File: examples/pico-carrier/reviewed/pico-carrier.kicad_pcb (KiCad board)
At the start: 2 copper layers, 88 x 62 mm, 9 parts, among them J1 5V IN, J3 GP0-GP15, J4 GP16-GP28, PWR, U1 Pico

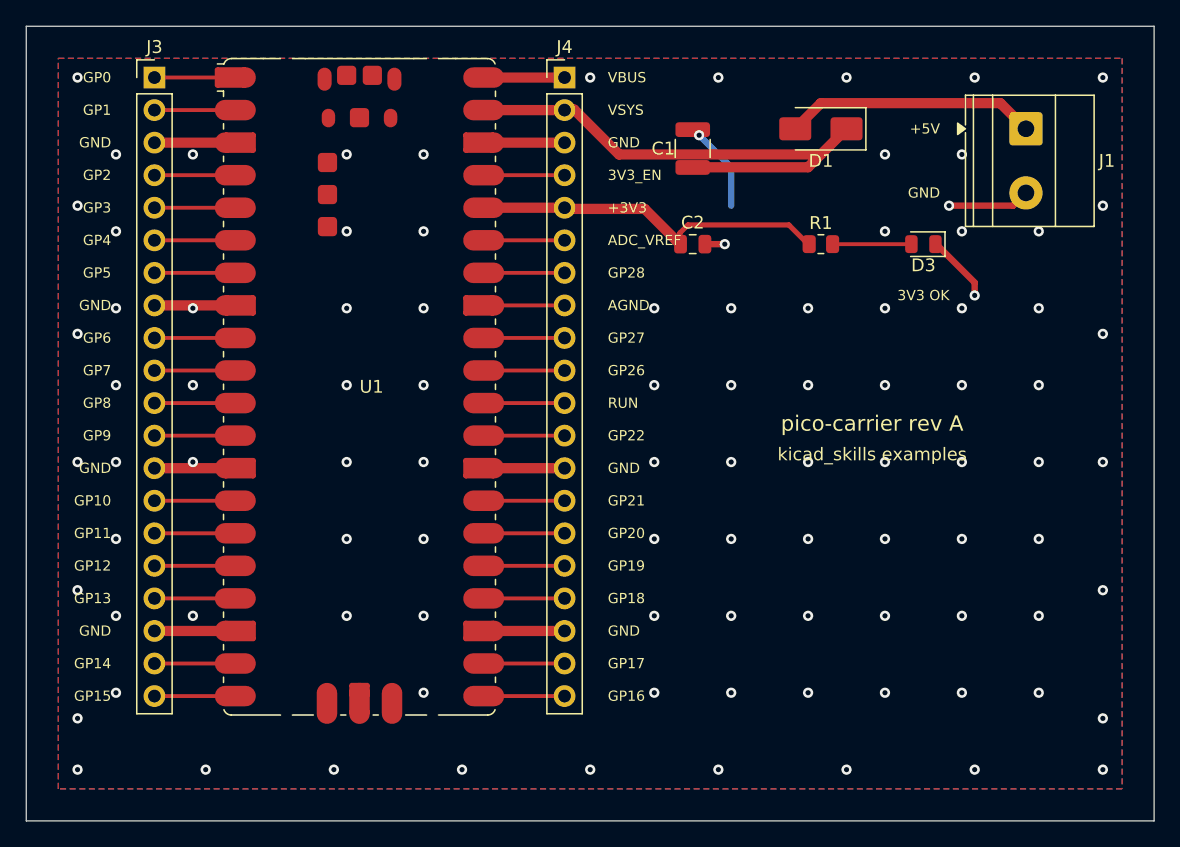
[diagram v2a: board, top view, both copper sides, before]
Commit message: Learn the drawing from the boards people drew
The brief for this round: relying on the autorouter and the numbers alone is
not enough - organise what pictorial correctness looks like from ordinary
circuits and open designs, and improve the drawing itself. So it starts in
KiCad's own demo corpus, measured and looked at, and ends with the habits
pushed into the generator.

tools/board_signature.py (new) reduces "looks autorouted" to five numbers.
Hand-routed two-layer boards cluster tightly: 10-47% of copper on the second
face, median segments 1.8-3.5 mm, 9-25 corners per decimetre, 91-98% of them
45s, 0.3-16 vias per decimetre. Rendering interf_u beside our boards says the
same thing in one glance: a layer has a direction, a bus travels as a bundle,
a person covers an offset with the long straight and one diagonal.

Three habits, now in the generator:

* Router.route(follow=...): cells beside a sibling net's path are discounted,
  so a bus (nets sharing a name prefix - I2S_*, SPI_*) travels as parallel
  lanes in one corridor. The discount is a fraction of a step, so it never
  buys a detour.
* _doglegged: every wiggly stretch is redrawn as the human stroke - the
  straight along the dominant direction plus one 45 - when the dogleg is
  clear, recursing into halves where a crossing blocks the whole. The op-amp
  board's median segment rose from 0.75 mm and its corner rate fell from
  38/dm; the FPGA board landed at 1.54 mm and 17.8/dm, inside the human band.
* Purposeful stitching: the 6 mm via carpet is gone. A ring at the rim, vias
  beside every back-layer crossing (where the plane is actually cut), and a
  coarse 12 mm mesh so no pour orphans. Vias/dm: buck 41 -> 18, carrier
  28 -> 13, all five inside the corpus band, pour_fragmented still silent.

Three failures the round produced and what they taught:

* pinned(): reshaping may not move copper off any point inside an own-net
  pad - the centre alone was not enough, a routed run touches off-centre and
  the ove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
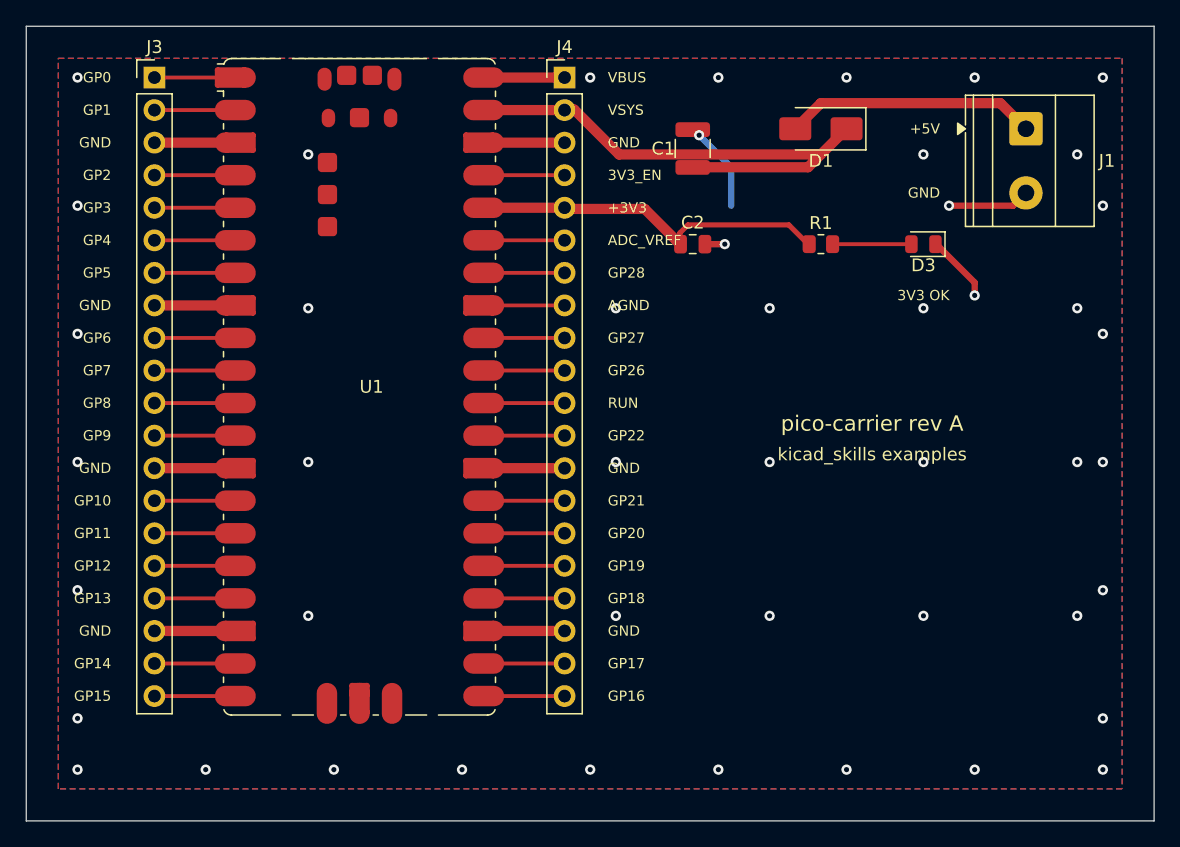
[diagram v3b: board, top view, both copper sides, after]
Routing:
- net GND: vias 98 -> 47
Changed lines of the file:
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@@
 	(via (at 104.0 114.0) (size 0.8) (drill 0.4) (layers "F.Cu" "B.Cu") (net 1))
 	(via (at 184.0 114.0) (size 0.8) (drill 0.4) (layers "F.Cu" "B.Cu") (net 1))
-	(via (at 107.0 70.0) (size 0.8) (drill 0.4) (layers "F.Cu" "B.Cu") (net 1))
-	(via (at 113.0 70.0) (size 0.8) (drill 0.4) (layers "F.Cu" "B.Cu") (net 1))
-	(via (at 125.0 70.0) (size 0.8) (drill 0.4) (layers "F.Cu" "B.Cu") (net 1))
-	(via (at 131.0 70.0) (size 0.8) (drill 0.4) (layers "F.Cu" "B.Cu") (net 1))
-	(via (at 167.0 70.0) (size 0.8) (drill 0.4) (layers "F.Cu" "B.Cu") (net 1))
-	(via (at 173.0 70.0) (size 0.8) (drill 0.4) (layers "F.Cu" "B.Cu") (net 1))
-	(via (at 107.0 76.0) (size 0.8) (drill 0.4) (layers "F.Cu" "B.Cu") (net 1))
-	(via (at 125.0 76.0) (size 0.8) (drill 0.4) (layers "F.Cu" "B.Cu") (net 1))
-	(via (at 131.0 76.0) (size 0.8) (drill 0.4) (layers "F.Cu" "B.Cu") (net 1))
-	(via (at 167.0 76.0) (size 0.8) (drill 0.4) (layers "F.Cu" "B.Cu") (net 1))
-	(via (at 173.0 76.0) (size 0.8) (drill 0.4) (layers "F.Cu" "B.Cu") (net 1))
-	(via (at 179.0 76.0) (size 0.8) (drill 0.4) (layers "F.Cu" "B.Cu") (net 1))
-	(via (at 107.0 82.0) (size 0.8) (drill 0.4) (layers "F.Cu" "B.Cu") (net 1))
-	(via (at 113.0 82.0) (size 0.8) (drill 0.4) (layers "F.Cu" "B.Cu") (net 1))
-	(via (at 125.0 82.0) (size 0.8) (drill 0.4) (layers "F.Cu" "B.Cu") (net 1))
-	(via (at 131.0 82.0) (size 0.8) (drill 0.4) (layers "F.Cu" "B.Cu") (net 1))
-	(via (at 149.0 82.0) (size 0.8) (drill 0.4) (layers "F.Cu" "B.Cu") (net 1))
-	(via (at 155.0 82.0) (size 0.8) (drill 0.4) (layers "F.Cu" "B.Cu") (net 1))
-	(via (at 161.0 82.0) (size 0.8) (drill 0.4) (layers "F.Cu" "B.Cu") (net 1))
-	(via (at 167.0 82.0) (size 0.8) (drill 0.4) (layers "F.Cu" "B.Cu") (net 1))
-	(via (at 173.0 82.0) (size 0.8) (drill 0.4) (layers "F.Cu" "B.Cu") (net 1))
-	(via (at 179.0 82.0) (size 0.8) (drill 0.4) (layers "F.Cu" "B.Cu") (net 1))
-	(via (at 107.0 88.0) (size 0.8) (drill 0.4) (layers "F.Cu" "B.Cu") (net 1))
-	(via (at 113.0 88.0) (size 0.8) (drill 0.4) (layers "F.Cu" "B.Cu") (net 1))
-	(via (at 125.0 88.0) (size 0.8) (drill 0.4) (layers "F.Cu" "B.Cu") (net 1))
-	(via (at 131.0 88.0) (size 0.8) (drill 0.4) (layers "F.Cu" "B.Cu") (net 1))
-	(via (at 149.0 88.0) (size 0.8) (drill 0.4) (layers "F.Cu" "B.Cu") (net 1))
-	(via (at 155.0 88.0) (size 0.8) (drill 0.4) (layers "F.Cu" "B.Cu") (net 1))
-	(via (at 161.0 88.0) (size 0.8) (drill 0.4) (layers "F.Cu" "B.Cu") (net 1))
-	(via (at 167.0 88.0) (size 0.8) (drill 0.4) (layers "F.Cu" "B.Cu") (net 1))
-	(via (at 173.0 88.0) (size 0.8) (drill 0.4) (layers "F.Cu" "B.Cu") (net 1))
-	(via (at 179.0 88.0) (size 0.8) (drill 0.4) (layers "F.Cu" "B.Cu") (net 1))
-	(via (at 107.0 94.0) (size 0.8) (drill 0.4) (layers "F.Cu" "B.Cu") (net 1))
-	(via (at 113.0 94.0) (size 0.8) (drill 0.4) (layers "F.Cu" "B.Cu") (net 1))
-	(via (at 125.0 94.0) (size 0.8) (drill 0.4) (layers "F.Cu" "B.Cu") (net 1))
-	(via (at 131.0 94.0) (size 0.8) (drill 0.4) (layers "F.Cu" "B.Cu") (net 1))
-	(via (at 149.0 94.0) (size 0.8) (drill 0.4) (layers "F.Cu" "B.Cu") (net 1))
-	(via (at 155.0 94.0) (size 0.8) (drill 0.4) (layers "F.Cu" "B.Cu") (net 1))
-	(via (at 161.0 94.0) (size 0.8) (drill 0.4) (layers "F.Cu" "B.Cu") (net 1))
-	(via (at 167.0 94.0) (size 0.8) (drill 0.4) (layers "F.Cu" "B.Cu") (net 1))
-	(via (at 173.0 94.0) (size 0.8) (drill 0.4) (layers "F.Cu" "B.Cu") (net 1))
-	(via (at 179.0 94.0) (size 0.8) (drill 0.4) (layers "F.Cu" "B.Cu") (net 1))
-	(via (at 107.0 100.0) (size 0.8) (drill 0.4) (layers "F.Cu" "B.Cu") (net 1))
-	(via (at 125.0 100.0) (size 0.8) (drill 0.4) (layers "F.Cu" "B.Cu") (net 1))
-	(via (at 131.0 100.0) (size 0.8) (drill 0.4) (layers "F.Cu" "B.Cu") (net 1))
-	(via (at 149.0 100.0) (size 0.8) (drill 0.4) (layers "F.Cu" "B.Cu") (net 1))
-	(via (at 155.0 100.0) (size 0.8) (drill 0.4) (layers "F.Cu" "B.Cu") (net 1))
-	(via (at 161.0 100.0) (size 0.8) (drill 0.4) (layers "F.Cu" "B.Cu") (net 1))
-	(via (at 167.0 100.0) (size 0.8) (drill 0.4) (layers "F.Cu" "B.Cu") (net 1))
-	(via (at 173.0 100.0) (size 0.8) (drill 0.4) (layers "F.Cu" "B.Cu") (net 1))
-	(via (at 179.0 100.0) (size 0.8) (drill 0.4) (layers "F.Cu" "B.Cu") (net 1))
-	(via (at 107.0 106.0) (size 0.8) (drill 0.4) (layers "F.Cu" "B.Cu") (net 1))
-	(via (at 113.0 106.0) (size 0.8) (drill 0.4) (layers "F.Cu" "B.Cu") (net 1))
-	(via (at 125.0 106.0) (size 0.8) (drill 0.4) (layers "F.Cu" "B.Cu") (net 1))
-	(via (at 131.0 106.0) (size 0.8) (drill 0.4) (layers "F.Cu" "B.Cu") (net 1))
-	(via (at 149.0 106.0) (size 0.8) (drill 0.4) (layers "F.Cu" "B.Cu") (net 1))
-	(via (at 155.0 106.0) (size 0.8) (drill 0.4) (layers "F.Cu" "B.Cu") (net 1))
-	(via (at 161.0 106.0) (size 0.8) (drill 0.4) (layers "F.Cu" "B.Cu") (net 1))
-	(via (at 167.0 106.0) (size 0.8) (drill 0.4) (layers "F.Cu" "B.Cu") (net 1))
-	(via (at 173.0 106.0) (size 0.8) (drill 0.4) (layers "F.Cu" "B.Cu") (net 1))
-	(via (at 179.0 106.0) (size 0.8) (drill 0.4) (layers "F.Cu" "B.Cu") (net 1))
-	(via (at 107.0 112.0) (size 0.8) (drill 0.4) (layers "F.Cu" "B.Cu") (net 1))
-	(via (at 131.0 112.0) (size 0.8) (drill 0.4) (layers "F.Cu" "B.Cu") (net 1))
-	(via (at 149.0 112.0) (size 0.8) (drill 0.4) (layers "F.Cu" "B.Cu") (net 1))
-	(via (at 155.0 112.0) (size 0.8) (drill 0.4) (layers "F.Cu" "B.Cu") (net 1))
-	(via (at 161.0 112.0) (size 0.8) (drill 0.4) (layers "F.Cu" "B.Cu") (net 1))
-	(via (at 167.0 112.0) (size 0.8) (drill 0.4) (layers "F.Cu" "B.Cu") (net 1))
-	(via (at 173.0 112.0) (size 0.8) (drill 0.4) (layers "F.Cu" "B.Cu") (net 1))
-	(via (at 179.0 112.0) (size 0.8) (drill 0.4) (layers "F.Cu" "B.Cu") (net 1))
+	(via (at 122.0 70.0) (size 0.8) (drill 0.4) (layers "F.Cu" "B.Cu") (net 1))
+	(via (at 170.0 70.0) (size 0.8) (drill 0.4) (layers "F.Cu" "B.Cu") (net 1))
+	(via (at 182.0 70.0) (size 0.8) (drill 0.4) (layers "F.Cu" "B.Cu") (net 1))
+	(via (at 122.0 82.0) (size 0.8) (drill 0.4) (layers "F.Cu" "B.Cu") (net 1))
+	(via (at 146.0 82.0) (size 0.8) (drill 0.4) (layers "F.Cu" "B.Cu") (net 1))
+	(via (at 158.0 82.0) (size 0.8) (drill 0.4) (layers "F.Cu" "B.Cu") (net 1))
+	(via (at 170.0 82.0) (size 0.8) (drill 0.4) (layers "F.Cu" "B.Cu") (net 1))
+	(via (at 182.0 82.0) (size 0.8) (drill 0.4) (layers "F.Cu" "B.Cu") (net 1))
+	(via (at 122.0 94.0) (size 0.8) (drill 0.4) (layers "F.Cu" "B.Cu") (net 1))
+	(via (at 146.0 94.0) (size 0.8) (drill 0.4) (layers "F.Cu" "B.Cu") (net 1))
+	(via (at 158.0 94.0) (size 0.8) (drill 0.4) (layers "F.Cu" "B.Cu") (net 1))
+	(via (at 170.0 94.0) (size 0.8) (drill 0.4) (layers "F.Cu" "B.Cu") (net 1))
+	(via (at 182.0 94.0) (size 0.8) (drill 0.4) (layers "F.Cu" "B.Cu") (net 1))
+	(via (at 122.0 106.0) (size 0.8) (drill 0.4) (layers "F.Cu" "B.Cu") (net 1))
+	(via (at 146.0 106.0) (size 0.8) (drill 0.4) (layers "F.Cu" "B.Cu") (net 1))
+	(via (at 158.0 106.0) (size 0.8) (drill 0.4) (layers "F.Cu" "B.Cu") (net 1))
+	(via (at 170.0 106.0) (size 0.8) (drill 0.4) (layers "F.Cu" "B.Cu") (net 1))
+	(via (at 182.0 106.0) (size 0.8) (drill 0.4) (layers "F.Cu" "B.Cu") (net 1))
 	(zone
 		(net 1)

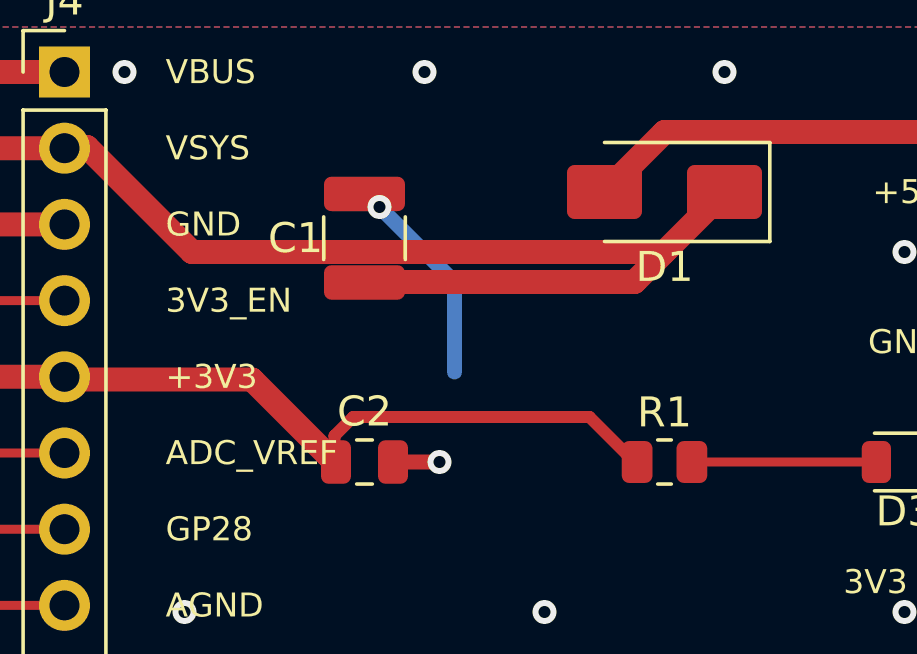
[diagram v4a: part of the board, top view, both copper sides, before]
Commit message: Let a link finish on its own net's copper instead of the pad it names
Every junction on these boards sat on a pad, because a pad was the only
place the router was allowed to stop: a net with three branches funnelled
all three into one 0402, and the reviewer circled the result - converging
diagonals meeting on C15. People do not draw that; they tap the trunk at
the nearest point.

So the search may now end on any cell whose centre lies exactly on the
net's own copper (a tee), with two guards that took one broken board each
to learn: only copper already joined to the link's endpoint counts, or the
named pad is left unconnected; and only a pad-named endpoint may be teed
away from, because a link aimed at a bare coordinate is aimed at the
stated end of a trunk someone drew, and stopping short strands the
trunk's tail. A landing mid-segment is inserted into the trunk's points as
a stated corner, so the reshaping passes pin the join like any other.

The op-amp board shows the effect: 12% less copper, fewer corners, longer
strokes, same connectivity - DRC clean, gates clean, zero crossings on all
four regenerated boards.

Co-Authored-By: Claude Fable 5 <noreply@anthropic.com>
Claude-Session: https://claude.ai/code/session_01DUj7Ltu92tWg159mCSacwY
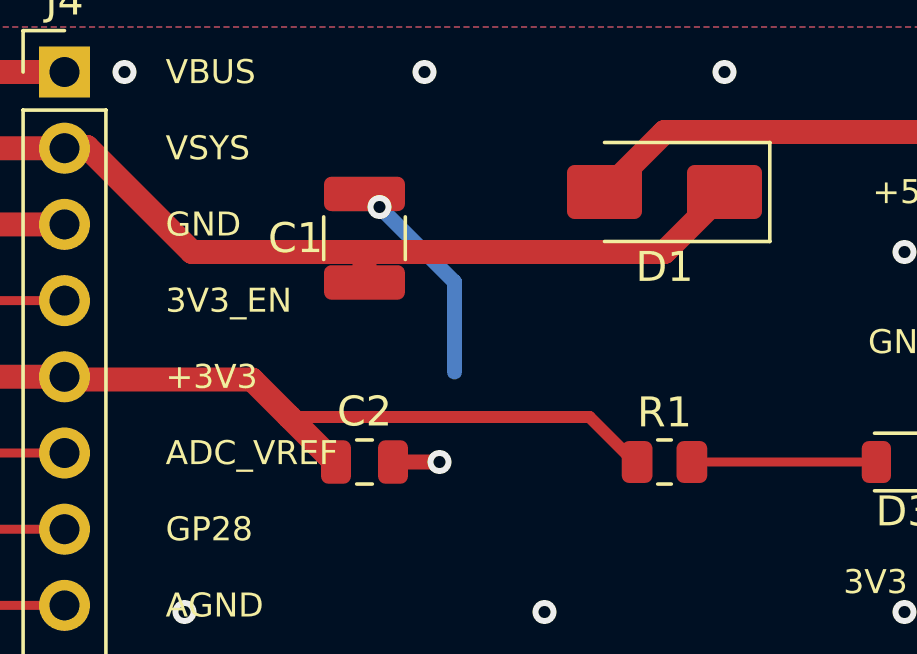
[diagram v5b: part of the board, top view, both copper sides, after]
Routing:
- net /VSYS: track 41.0 -> 31.6 mm
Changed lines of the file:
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@@
 	(segment (start 142.25 66.5) (end 142.75 66.5) (width 0.8) (layer "F.Cu") (net 36))
 	(segment (start 142.75 66.5) (end 146.25 70.0) (width 0.8) (layer "F.Cu") (net 36))
-	(segment (start 146.25 70.0) (end 162.0 70.0) (width 0.8) (layer "F.Cu") (net 36))
+	(segment (start 146.25 70.0) (end 152.0 70.0) (width 0.8) (layer "F.Cu") (net 36))
 	(segment (start 135.69 71.62) (end 142.0 71.62) (width 0.3) (layer "F.Cu") (net 4))
 	(segment (start 135.69 74.16) (end 142.0 74.16) (width 0.8) (layer "F.Cu") (net 2))
@@
 	(segment (start 142.09 74.25) (end 142.25 74.25) (width 0.8) (layer "F.Cu") (net 2))
 	(segment (start 142.25 74.25) (end 148.25 74.25) (width 0.8) (layer "F.Cu") (net 2))
-	(segment (start 148.25 74.25) (end 150.75 76.75) (width 0.8) (layer "F.Cu") (net 2))
-	(segment (start 150.75 76.75) (end 151.0 77.0) (width 0.8) (layer "F.Cu") (net 2))
-	(segment (start 151.0 77.0) (end 151.05 77.0) (width 0.8) (layer "F.Cu") (net 2))
+	(segment (start 148.25 74.25) (end 149.5 75.5) (width 0.8) (layer "F.Cu") (net 2))
 	(segment (start 135.69 76.7) (end 142.0 76.7) (width 0.3) (layer "F.Cu") (net 5))
 	(segment (start 135.69 79.24) (end 142.0 79.24) (width 0.3) (layer "F.Cu") (net 25))
@@
 	(segment (start 176.0 66.0) (end 162.0 66.0) (width 0.8) (layer "F.Cu") (net 3))
 	(segment (start 162.0 66.0) (end 160.0 68.0) (width 0.8) (layer "F.Cu") (net 3))
-	(segment (start 152.0 71.015) (end 152.235 71.015) (width 0.8) (layer "F.Cu") (net 36))
-	(segment (start 152.235 71.015) (end 152.25 71.0) (width 0.8) (layer "F.Cu") (net 36))
-	(segment (start 152.25 71.0) (end 161.0 71.0) (width 0.8) (layer "F.Cu") (net 36))
-	(segment (start 161.0 71.0) (end 164.0 68.0) (width 0.8) (layer "F.Cu") (net 36))
-	(segment (start 151.05 77.0) (end 151.05 76.8) (width 0.4) (layer "F.Cu") (net 2))
-	(segment (start 151.05 76.8) (end 151.0 76.75) (width 0.4) (layer "F.Cu") (net 2))
-	(segment (start 151.0 76.75) (end 151.0 76.125) (width 0.4) (layer "F.Cu") (net 2))
-	(segment (start 151.0 76.125) (end 151.625 75.5) (width 0.4) (layer "F.Cu") (net 2))
-	(segment (start 151.625 75.5) (end 159.5 75.5) (width 0.4) (layer "F.Cu") (net 2))
-	(segment (start 159.5 75.5) (end 160.75 76.75) (width 0.4) (layer "F.Cu") (net 2))
-	(segment (start 160.75 76.75) (end 160.8375 76.75) (width 0.4) (layer "F.Cu") (net 2))
-	(segment (start 160.8375 76.75) (end 161.0875 77.0) (width 0.4) (layer "F.Cu") (net 2))
+	(segment (start 164.0 68.0) (end 162.0 70.0) (width 0.8) (layer "F.Cu") (net 36))
+	(segment (start 162.0 70.0) (end 152.0 70.0) (width 0.8) (layer "F.Cu") (net 36))
+	(segment (start 152.0 71.015) (end 152.0 70.0) (width 0.8) (layer "F.Cu") (net 36))
+	(segment (start 151.05 77.0) (end 151.0 77.0) (width 0.8) (layer "F.Cu") (net 2))
+	(segment (start 151.0 77.0) (end 150.75 76.75) (width 0.8) (layer "F.Cu") (net 2))
+	(segment (start 150.75 76.75) (end 149.5 75.5) (width 0.8) (layer "F.Cu") (net 2))
+	(segment (start 161.0875 77.0) (end 161.0 77.0) (width 0.4) (layer "F.Cu") (net 2))
+	(segment (start 161.0 77.0) (end 160.75 76.75) (width 0.4) (layer "F.Cu") (net 2))
+	(segment (start 160.75 76.75) (end 159.5 75.5) (width 0.4) (layer "F.Cu") (net 2))
+	(segment (start 159.5 75.5) (end 149.5 75.5) (width 0.4) (layer "F.Cu") (net 2))
 	(segment (start 162.9125 77.0) (end 169.0625 77.0) (width 0.3) (layer "F.Cu") (net 33))
 	(via (at 152.5 68.5) (size 0.8) (drill 0.4) (layers "F.Cu" "B.Cu") (net 1))
